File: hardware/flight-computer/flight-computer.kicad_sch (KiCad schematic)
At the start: 2 parts, among them U1 STM32F103C8Tx, U2 BME280

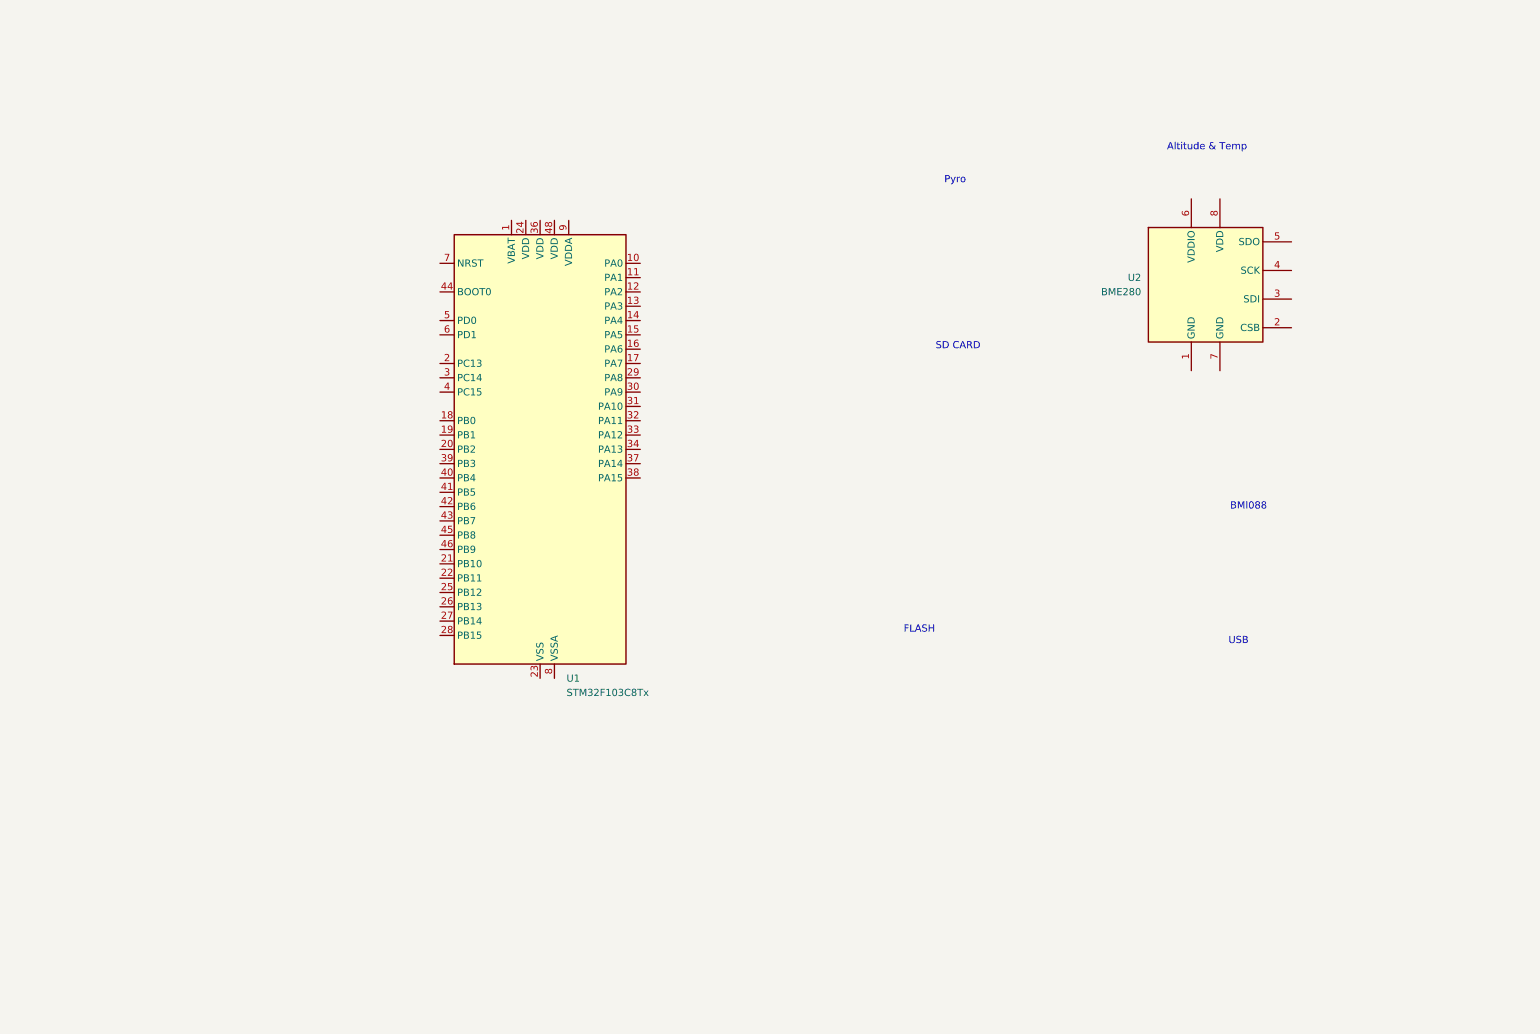
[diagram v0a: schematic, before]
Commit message: Layed out microcontroller and added some other circuit components.
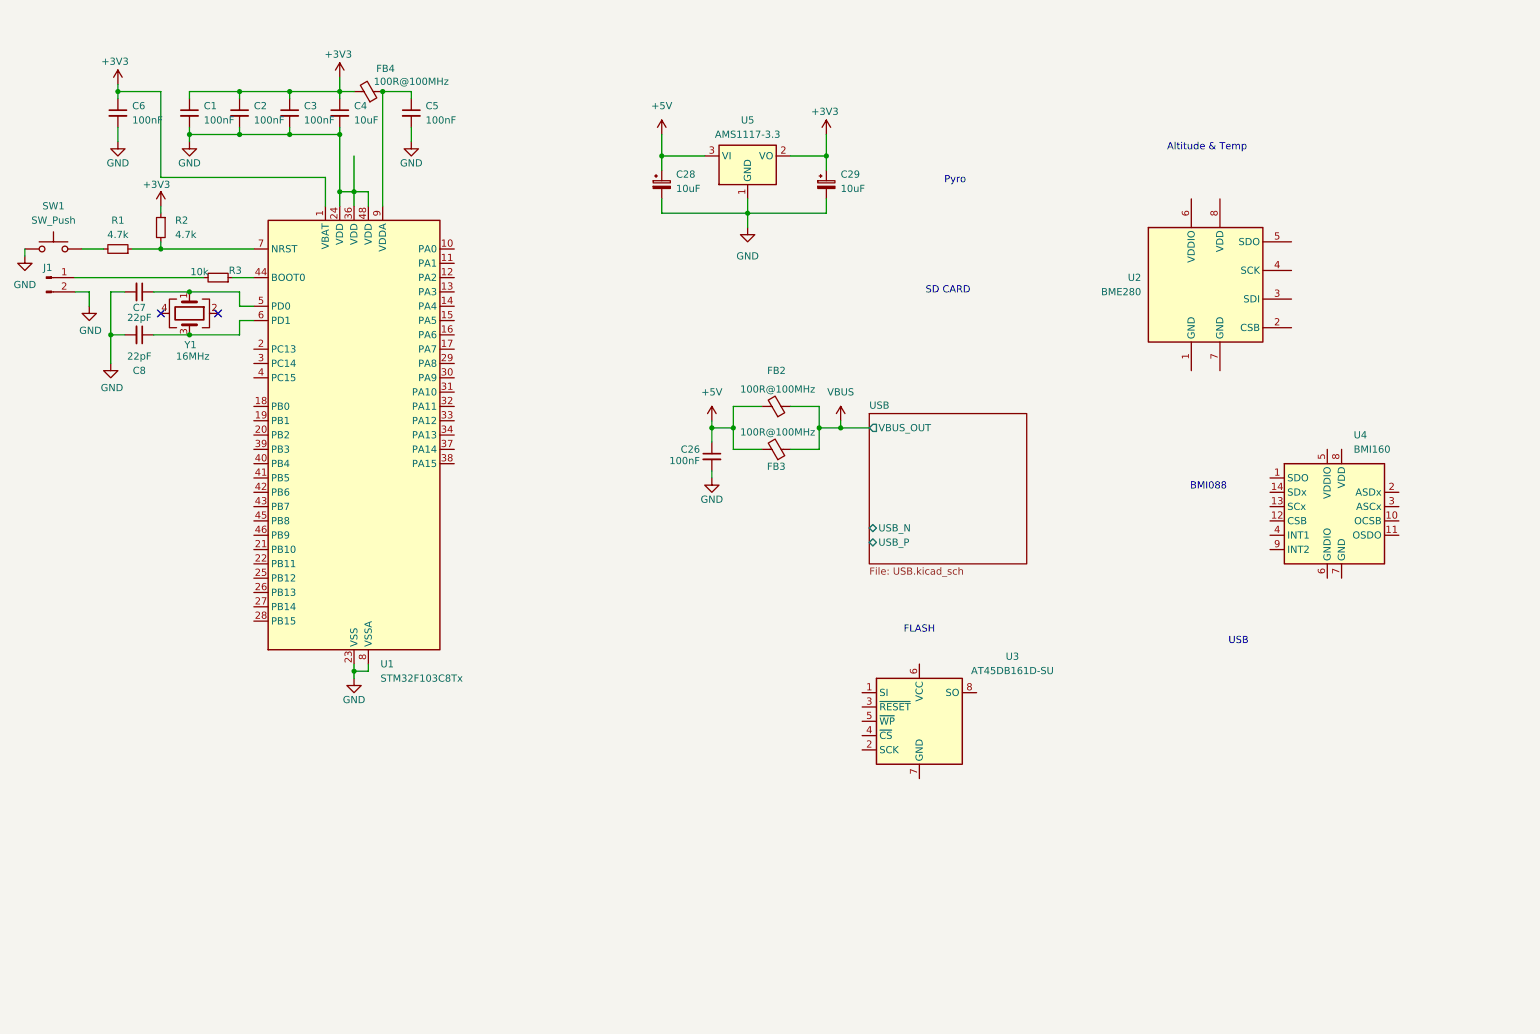
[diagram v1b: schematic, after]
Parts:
- added C1, C2, C26, C3, C5, C6: 100nF, Capacitor_SMD:C_0603_1608Metric, symbol Device:C_Small
- added C28, C29: 10uF, Capacitor_SMD:C_1206_3216Metric, symbol Device:C_Polarized_Small
- added C4: 10uF, Capacitor_SMD:C_1206_3216Metric, symbol Device:C_Small
- added C7, C8: 22pF, Capacitor_SMD:C_0603_1608Metric, symbol Device:C_Small
- added FB2, FB3, FB4: 100R@100MHz, Inductor_SMD:L_0603_1608Metric, symbol Device:FerriteBead_Small
- added J1: Conn_01x02_Pin, symbol Connector:Conn_01x02_Pin
- added R1, R2: 4.7k, Resistor_SMD:R_0603_1608Metric, symbol Device:R_Small
- added R3: 10k, Resistor_SMD:R_0603_1608Metric, symbol Device:R_Small
- added SW1: SW_Push, Button_Switch_SMD:SW_Push_1P1T_XKB_TS-1187A, symbol Switch:SW_Push
- added U3: AT45DB161D-SU, Package_SO:SOIC-28W_8.7x18.25mm_P1.27mm, symbol Memory_Flash:AT45DB161D-SU
- added U4: BMI160, Package_LGA:Bosch_LGA-14_3x2.5mm_P0.5mm, symbol Sensor_Motion:BMI160
- added U5: AMS1117-3.3, Package_TO_SOT_SMD:SOT-223-3_TabPin2, symbol Regulator_Linear:AMS1117-3.3
- added Y1: 16MHz, Crystal:Crystal_SMD_3225-4Pin_3.2x2.5mm, symbol Device:Crystal_GND24
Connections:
- net +3V3: now reaches U1.1 (VBAT)
- net +3V3: now also C1.1, C2.1, C29.1, C3.1, C4.1, C6.1, FB4.2, R2.1, U5.2 (VO)
- net GND: now reaches U1.23 (VSS), U1.35 (VSS), U1.47 (VSS)
- net GND: now also U1.24 (VDD), U1.36 (VDD), U1.48 (VDD), U1.8 (VSSA), C1.2, C2.2, C26.2, C28.2, C29.2, C3.2, C4.2, C5.2, C6.2, C7.2, C8.2, J1.2 (Pin_2), SW1.2, U5.1 (GND)
- net at U1.44 (BOOT0): now also R3.1
- net at U1.5 (PD0): now also C7.1, Y1.1
- net at U1.6 (PD1): now also C8.1, Y1.3
- net at U1.7 (NRST): now also R1.1, R2.2
- net at U1.9 (VDDA): now also C5.1, FB4.1
- new net: J1.1 (Pin_1), R3.2
- new net: R1.2, SW1.1
- new net +5V: C26.1, C28.1, FB2.2, FB3.2, U5.3 (VI)
- new net VBUS: FB2.1, FB3.1
- no-connect marks 0 -> 2
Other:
- added sheet USB (USB.kicad_sch)
- moved on the sheet: U1

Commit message: Added 9 axis IMU and other IMUs
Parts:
- removed R1, R2: 4.7k, Resistor_SMD:R_0603_1608Metric, symbol Device:R_Small
- added C10, C11, C12, C13, C9: 100nF, Capacitor_SMD:C_0603_1608Metric, symbol Device:C_Small
- added FB5, FB6: 100R@100MHz, Inductor_SMD:L_0603_1608Metric, symbol Device:FerriteBead_Small
- added R5, R6, R7, R8: 10k, Resistor_SMD:R_0603_1608Metric, symbol Device:R_Small
- added U6: ICM-20948, Sensor_Motion:InvenSense_QFN-24_3x3mm_P0.4mm, symbol Sensor_Motion:ICM-20948
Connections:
- net +3V3: now also U2.6 (VDDIO), U3.6 (VCC), U4.5 (VDDIO), C10.1, C12.1, C9.1, FB5.2, FB6.2, R5.1, R6.1, R7.1, R8.1
- net GND: now also U2.1 (GND), U2.7 (GND), U3.7 (GND), U4.6 (GNDIO), U4.7 (GND), C10.2, C11.2, C12.2, C13.2, C9.2
- net at SW1.1: now also U1.7 (NRST), R5.2
- net ALT_CS: now reaches U2.2 (CSB)
- net ALT_CS: now also R8.2
- net MCU_SDO: now reaches U2.3 (SDI)
- net MCU_SDO: now also U3.1 (SI)
- net MCU_SCK: now reaches U2.4 (SCK)
- net MCU_SCK: now also U3.2 (SCK)
- net MCU_SDI: now reaches U2.5 (SDO)
- net MCU_SDI: now also U3.8 (SO), U4.1 (SDO)
- net at U2.8 (VDD): now also C11.1, FB5.1
- net IMU_CS: now reaches U4.12 (CSB)
- net at U4.8 (VDD): now also C13.1, FB6.1
- net at U3.3 (~{RESET}): now also U3.5 (~{WP}), R6.2
- net FLASH_CS: now reaches U3.4 (~{CS})
- net FLASH_CS: now also R7.2
- new net: U6.18 (GND), U6.20 (GND)
- no-connect marks 2 -> 9
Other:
- note removed: "BMI088"
- moved on the sheet: C26, C28, C29, FB2, FB3, U2, U3, U4, U5

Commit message: removed old IMU
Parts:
- removed U4: BMI160, Package_LGA:Bosch_LGA-14_3x2.5mm_P0.5mm, symbol Sensor_Motion:BMI160
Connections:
- net +3V3: now also C13.1, FB6.1, U6.13 (VDD); no longer C12.1, FB6.2
- net GND: now also U6.18 (GND), U6.20 (GND)
- net IMU_CS: now also U6.22 (~{CS})
- net MCU_SDI: now also U6.9 (SDO/AD0)
- net at U6.8 (VDDIO): now also C12.1, FB6.2
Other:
- moved on the sheet: C12, C13, FB6, U6

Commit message: Added magnomiters
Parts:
- added U4: TLV493D, Package_TO_SOT_SMD:SOT-23-6, symbol Sensor_Magnetic:TLV493D
- added U7: LIS2MDL, Package_LGA:LGA-12_2x2mm_P0.5mm, symbol Sensor_Magnetic:LIS2MDL
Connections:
- new net: U7.6 (GND), U7.8 (GND)
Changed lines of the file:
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@@
 	)
 	(symbol
+		(lib_id "Sensor_Magnetic:TLV493D")
+		(at 195.58 97.79 0)
+		(unit 1)
+		(exclude_from_sim no)
+		(in_bom yes)
+		(on_board yes)
+		(dnp no)
+		(fields_autoplaced yes)
+		(property "Reference" "U4"
+			(at 203.2 95.2499 0)
+			(effects
+				(font
+					(size 1.27 1.27)
+				)
+				(justify left)
+			)
+		)
+		(property "Value" "TLV493D"
+			(at 203.2 97.7899 0)
+			(effects
+				(font
+					(size 1.27 1.27)
+				)
+				(justify left)
+			)
+		)
+		(property "Footprint" "Package_TO_SOT_SMD:SOT-23-6"
+			(at 194.31 110.49 0)
+			(effects
+				(font
+					(size 1.27 1.27)
+				)
+				(hide yes)
+			)
+		)
+		(property "Datasheet" "http://www.infineon.com/dgdl/Infineon-TLV493D-A1B6-DS-v01_00-EN.pdf?fileId=5546d462525dbac40152a6b85c760e80"
+			(at 191.77 85.09 0)
+			(effects
+				(font
+					(size 1.27 1.27)
+				)
+				(hide yes)
+			)
+		)
+		(property "Description" "Low power 3D magnetic sensor, I2C interface, SOT-23-6"
+			(at 195.58 97.79 0)
+			(effects
+				(font
+					(size 1.27 1.27)
+				)
+				(hide yes)
+			)
+		)
+		(pin "5"
+		)
+		(pin "1"
+		)
+		(pin "3"
+		)
+		(pin "6"
+		)
+		(pin "4"
+		)
+		(pin "2"
+		)
+		(instances
+			(project ""
+				(path "/2ecc7c5b-d66e-4f4b-a14e-df55f20aa743"
+					(reference "U4")
+					(unit 1)
+				)
+			)
+		)
+	)
+	(symbol
 		(lib_id "power:+5V")
 		(at 143.51 156.21 0)
@@
 					(unit 1)
 				)
+			)
+		)
+	)
+	(symbol
+		(lib_id "Sensor_Magnetic:LIS2MDL")
+		(at 152.4 101.6 0)
+		(unit 1)
+		(exclude_from_sim no)
+		(in_bom yes)
+		(on_board yes)
+		(dnp no)
+		(fields_autoplaced yes)
+		(property "Reference" "U7"
+			(at 154.5433 114.3 0)
+			(effects
+				(font
+					(size 1.27 1.27)
+				)
+				(justify left)
+			)
+		)
+		(property "Value" "LIS2MDL"
+			(at 154.5433 116.84 0)
+			(effects
+				(font
+					(size 1.27 1.27)
+				)
+				(justify left)
+			)
+		)
+		(property "Footprint" "Package_LGA:LGA-12_2x2mm_P0.5mm"
+			(at 182.88 109.22 0)
+			(effects
+				(font
+					(size 1.27 1.27)
+				)
+				(hide yes)
+			)
+		)
+		(property "Datasheet" "https://www.st.com/resource/en/datasheet/lis2mdl.pdf"
+			(at 190.5 111.76 0)
+			(effects
+				(font
+					(size 1.27 1.27)
+				)
+				(hide yes)
+			)
+		)
+		(property "Description" "Ultra-low-power, 3-axis digital output magnetometer, LGA-12"
+			(at 152.4 101.6 0)
+			(effects
+				(font
+					(size 1.27 1.27)
+				)
+				(hide yes)
+			)
+		)
+		(pin "2"
+		)
+		(pin "9"
+		)
+		(pin "3"
+		)
+		(pin "1"
+		)
+		(pin "4"
+		)
+		(pin "11"
+		)
+		(pin "7"
+		)
+		(pin "10"
+		)
+		(pin "5"
+		)
+		(pin "6"
+		)
+		(pin "8"
+		)
+		(pin "12"
+		)
+		(instances
+			(project ""
+				(path "/2ecc7c5b-d66e-4f4b-a14e-df55f20aa743"
+					(reference "U7")
+					(unit 1)
+				)

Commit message: Added new sensors
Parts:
- removed R7, R8: 10k, Resistor_SMD:R_0603_1608Metric, symbol Device:R_Small
- removed U2: BME280, Package_LGA:Bosch_LGA-8_2.5x2.5mm_P0.65mm_ClockwisePinNumbering, symbol Sensor:BME280
- removed U3: AT45DB161D-SU, Package_SO:SOIC-28W_8.7x18.25mm_P1.27mm, symbol Memory_Flash:AT45DB161D-SU
- removed U4: TLV493D, Package_TO_SOT_SMD:SOT-23-6, symbol Sensor_Magnetic:TLV493D
- removed U6: ICM-20948, Sensor_Motion:InvenSense_QFN-24_3x3mm_P0.4mm, symbol Sensor_Motion:ICM-20948
- removed U7: LIS2MDL, Package_LGA:LGA-12_2x2mm_P0.5mm, symbol Sensor_Magnetic:LIS2MDL
- added C14, C15: 100nF, Capacitor_SMD:C_0603_1608Metric, symbol Device:C_Small
- added C16: 220nF, Capacitor_SMD:C_0603_1608Metric, symbol Device:C_Small
- added FB1: 100R@100MHz, Inductor_SMD:L_0603_1608Metric, symbol Device:FerriteBead_Small
- added R1: 10k, Resistor_SMD:R_0603_1608Metric, symbol Device:R_Small
- added U2: LIS2MDL, Package_LGA:LGA-12_2x2mm_P0.5mm, symbol Sensor_Magnetic:LIS2MDL
- added U3: BMP588, symbol symbols:BMP580
- added U8: W25Q128JVS, Package_SO:SOIC-8_5.3x5.3mm_P1.27mm, symbol Memory_Flash:W25Q128JVS
- added U9: LSM6DS3, Package_LGA:LGA-14_3x2.5mm_P0.5mm_LayoutBorder3x4y, symbol Sensor_Motion:LSM6DS3
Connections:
- net +3V3: now also C12.1, FB6.2, C14.1, FB1.2, R1.1, U2.9 (Vdd), U3.1 (VDDIO), U8.8 (VCC), U9.5 (VDDIO); no longer C13.1, FB6.1
- net ALT_CS: now also U3.6 (nCS)
- net FLASH_CS: now also U8.1 (~{CS})
- net GND: now also C14.2, C15.2, C16.2, U2.6 (GND), U2.8 (GND), U3.3 (VSS), U3.8 (VSS), U3.9 (VSS), U8.4 (GND), U9.6 (GND), U9.7 (GND)
- net IMU_CS: now also U9.12 (CS)
- net MCU_SCK: now also U8.6 (CLK), U9.13 (SCL)
- net MCU_SDI: now also U8.2 (DO/IO_{1}), U9.1 (SDO/SA0)
- net MCU_SDO: now also U8.5 (DI/IO_{0}), U9.14 (SDA)
- net at C11.1, FB5.1: now also U3.10 (VDD)
- net at R6.2: now also U8.3 (~{WP}/IO_{2})
- new net: C16.1, U2.5 (C1)
- new net: C13.1, FB6.1, U9.8 (VDD)
- new net: C15.1, FB1.1, U2.10 (Vdd_IO)
- new net: R1.2, U8.7 (~{HOLD}/~{RESET}/IO_{3})
- new net MAG_CS: U2.3 (~{CS})
- new net MCU_I2C_SCL: U2.1 (SCL/SPC), U3.2 (SCK)
- new net MCU_I2C_SDA: U2.4 (SDA/SDI/SDO), U3.4 (SDI)
- no-connect marks 9 -> 12
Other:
- note added: "ACCELEROMETER"
- note added: "COMPASS"
- moved on the sheet: C10, C11, C12, C13, C26, C9, FB2, FB3, FB5, FB6, R6

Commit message: Worked on schematic allocated more serial busses, just gpio to go
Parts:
- removed C10, C11, C12, C13, C14, C15, C9: 100nF, Capacitor_SMD:C_0603_1608Metric, symbol Device:C_Small
- removed C16: 220nF, Capacitor_SMD:C_0603_1608Metric, symbol Device:C_Small
- removed FB1, FB5, FB6: 100R@100MHz, Inductor_SMD:L_0603_1608Metric, symbol Device:FerriteBead_Small
- removed R1, R6: 10k, Resistor_SMD:R_0603_1608Metric, symbol Device:R_Small
- removed U2: LIS2MDL, Package_LGA:LGA-12_2x2mm_P0.5mm, symbol Sensor_Magnetic:LIS2MDL
- removed U3: BMP588, symbol symbols:BMP580
- removed U8: W25Q128JVS, Package_SO:SOIC-8_5.3x5.3mm_P1.27mm, symbol Memory_Flash:W25Q128JVS
- removed U9: LSM6DS3, Package_LGA:LGA-14_3x2.5mm_P0.5mm_LayoutBorder3x4y, symbol Sensor_Motion:LSM6DS3
- added R11, R12, R13, R2: 10k, Resistor_SMD:R_0603_1608Metric, symbol Device:R_Small
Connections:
- net +3V3: now also R11.1, R12.1, R13.1, R2.1
- net FLASH_CS: now also U1.25 (PB12)
- net IMU_CS: now also U1.14 (PA4)
- net MCU_SCK1: now reaches U1.15 (PA5)
- net MCU_SDI1: now reaches U1.16 (PA6)
- net MCU_SDO1: now reaches U1.17 (PA7)
- net MCU_SCL2: now reaches U1.21 (PB10)
- net MCU_SCL2: now also R12.2
- net MCU_SDA2: now reaches U1.22 (PB11)
- net MCU_SDA2: now also R13.2
- net MCU_SCK2: now reaches U1.26 (PB13)
- net MCU_SDI2: now reaches U1.27 (PB14)
- net MCU_SDO2: now reaches U1.28 (PB15)
- net UART1_RX: now reaches U1.31 (PA10)
- net UART1_TX: now reaches U1.32 (PA11)
- net MCU_SCL1: now reaches U1.42 (PB6)
- net MCU_SCL1: now also R2.2
- net MCU_SDA1: now reaches U1.43 (PB7)
- net MCU_SDA1: now also R11.2
- no-connect marks 12 -> 5
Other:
- added sheet Memory (memory.kicad_sch)
- added sheet Sensors (sensors.kicad_sch)
- note removed: "ACCELEROMETER"
- note removed: "Altitude & Temp"
- note removed: "COMPASS"
- note removed: "FLASH"
- note removed: "SD CARD"
- note removed: "USB"
- moved on the sheet: C1, C2, C26, C28, C29, C3, C4, C5, C6, C7, C8, FB2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

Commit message: Worked on tidy up just pyro and sd card to go
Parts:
- added J3, J4: Conn_01x03_Pin, symbol Connector:Conn_01x03_Pin
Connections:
- net +5V: now also J3.2 (Pin_2), J4.2 (Pin_2)
- net GND: now also J3.1 (Pin_1), J4.1 (Pin_1)
- net UART1_TX: now also U1.30 (PA9); no longer U1.32 (PA11)
- net 1PPS: now reaches U1.10 (PA0)
- net PYRO_1: now reaches U1.11 (PA1)
- net PYRO_2: now reaches U1.12 (PA2)
- net SERVO_1: now reaches U1.18 (PB0)
- net SERVO_1: now also J3.3 (Pin_3)
- net SERVO_2: now reaches U1.19 (PB1)
- net SERVO_2: now also J4.3 (Pin_3)
- net USB_P: now reaches U1.33 (PA12)
- net PYRO_ICHECK_2: now reaches U1.38 (PA15)
- net PYRO_ICHECK_2: now also U1.39 (PB3)
- new net USB_N: U1.32 (PA11)
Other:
- added sheet Pryo (pyro.kicad_sch)
- sheet Memory ports: added MCU_SCK, MCU_SDI, MCU_SDO; removed SCK, SDI, SDO
- sheet Sensors ports: added BAR_SCL, BAR_SDA, IMU_CS, MAG_SCL, MAG_SDA, MCU_SCK, MCU_SDI, MCU_SDO; removed none
- note added: "SERVO CONTROL"
- moved on the sheet: C26, C6, FB2, FB3, J1, R11, R12, R13, R2, R5, SW1
